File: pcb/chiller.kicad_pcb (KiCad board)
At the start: 2 copper layers, 62.2 x 55.1 mm, 45 parts, among them J1 CONN_01X03, J10 CONN_01X03, J11 CONN_01X02, J12 CONN_01X02, J2 CONN_01X03, J3 CONN_01X03, J4 CONN_01X02, J5 CONN_01X02, J6 CONN_01X02, J7 CONN_01X02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

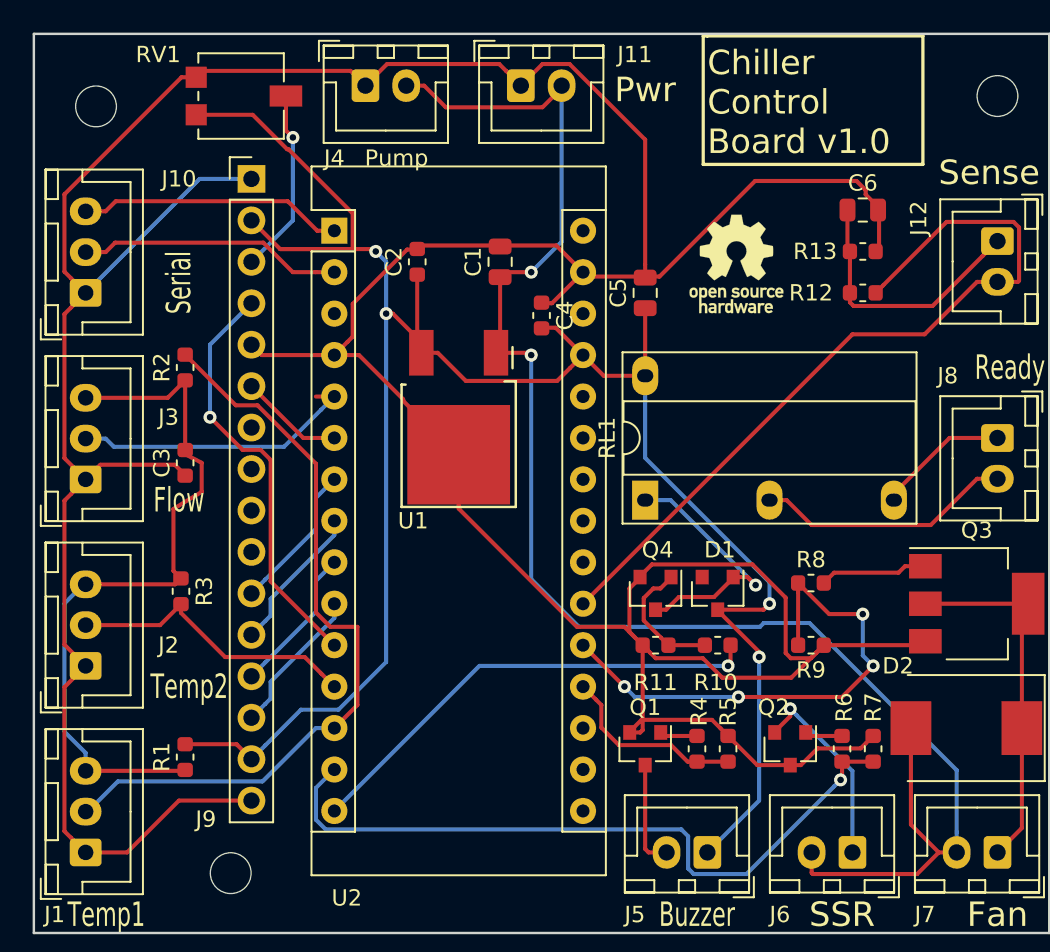
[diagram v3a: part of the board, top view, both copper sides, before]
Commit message: Fix errors: - Relay wrong footprint - Q2 switched D and G
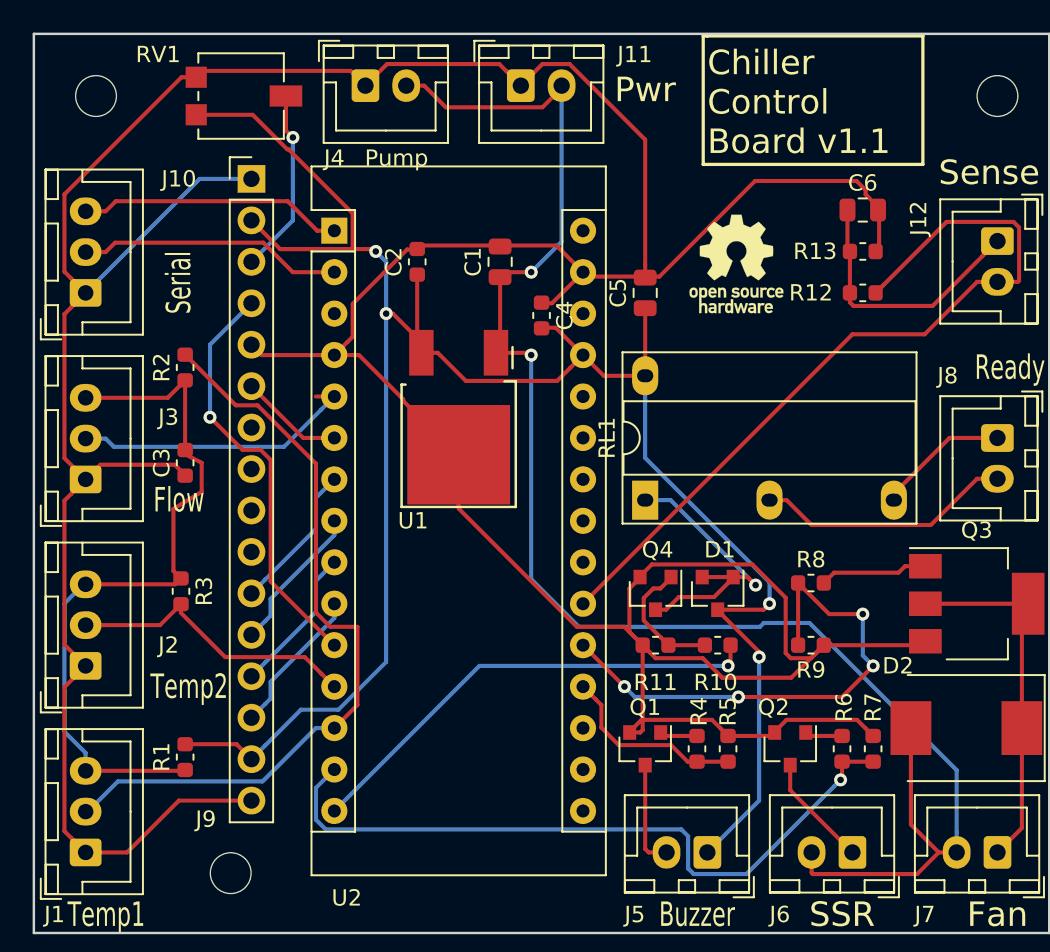
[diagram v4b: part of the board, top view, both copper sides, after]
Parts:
- moved REF** 0.64 mm to (183.5, 52.7)
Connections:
- D1 pad 2: (no net) -> Net-(D1-Pad1)
- Q2 pad 2: Net-(J6-Pad1) -> GND
- Q2 pad 3: GND -> Net-(J6-Pad1)
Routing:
- net Net-(J6-Pad1): track 12.2 -> 6.93 mm, vias 1 -> 0
- net Net-(D1-Pad1): track 16.1 -> 18.0 mm
- net GND: track 270.3 -> 269.7 mm
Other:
- rule pad_to_mask_clearance: 0.2 -> -0.2
- board text added: "Chiller Control Board v1.1"
- board text removed: "Chiller Control Board v1.0"
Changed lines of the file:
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@@
-(kicad_pcb (version 20171130) (host pcbnew 5.0.0-fee4fd1~66~ubuntu16.04.1)
+(kicad_pcb (version 20171130) (host pcbnew 5.0.2-bee76a0~70~ubuntu18.04.1)
   (general
     (thickness 1.6)
     (drawings 22)
-    (tracks 392)
+    (tracks 388)
     (zones 0)
     (modules 45)
@@
   (page A4)
   (layers
-    (0 F.Cu signal hide)
+    (0 F.Cu signal)
     (31 B.Cu signal)
     (32 B.Adhes user)
@@
     (pad_size 1.524 1.524)
     (pad_drill 0.762)
-    (pad_to_mask_clearance 0.2)
+    (pad_to_mask_clearance -0.2)
+    (solder_mask_min_width 0.25)
     (aux_axis_origin 0 0)
     (visible_elements FFFFFF7F)
     (pcbplotparams
-      (layerselection 0x010fc_ffffffff)
+      (layerselection 0x00008_7ffffffe)
       (usegerberextensions false)
       (usegerberattributes false)
@@
       (padsonsilk false)
       (subtractmaskfromsilk false)
-      (outputformat 1)
+      (outputformat 5)
       (mirror false)
       (drillshape 0)
@@
     (pad 3 smd rect (at 1 0 270) (size 0.9 0.8) (layers F.Cu F.Paste F.Mask)
       (net 3 +5V))
-    (pad 2 smd rect (at -1 0.95 270) (size 0.9 0.8) (layers F.Cu F.Paste F.Mask))
+    (pad 2 smd rect (at -1 0.95 270) (size 0.9 0.8) (layers F.Cu F.Paste F.Mask)
+      (net 24 "Net-(D1-Pad1)"))
     (pad 1 smd rect (at -1 -0.95 270) (size 0.9 0.8) (layers F.Cu F.Paste F.Mask)
       (net 24 "Net-(D1-Pad1)"))
@@
       (net 29 "Net-(Q2-Pad1)"))
     (pad 2 smd rect (at -1 0.95 270) (size 0.9 0.8) (layers F.Cu F.Paste F.Mask)
+      (net 1 GND))
+    (pad 3 smd rect (at 1 0 270) (size 0.9 0.8) (layers F.Cu F.Paste F.Mask)
       (net 26 "Net-(J6-Pad1)"))
-    (pad 3 smd rect (at 1 0 270) (size 0.9 0.8) (layers F.Cu F.Paste F.Mask)
-      (net 1 GND))
     (model ${KISYS3DMOD}/Package_TO_SOT_SMD.3dshapes/SOT-23.wrl
       (at (xyz 0 0 0))
@@
   )
   (module MountingHole:MountingHole_2.5mm (layer F.Cu)
-    (at 183.515 53.34)
+    (at 183.515 52.705)
     (descr "Mounting Hole 2.5mm, no annular")
     (tags "mounting hole 2.5mm no annular")
@@
   (gr_line (start 234.188 49.022) (end 234.188 56.896) (layer F.SilkS) (width 0.2))
   (gr_line (start 220.98 49.022) (end 234.188 49.022) (layer F.SilkS) (width 0.2))
-  (gr_text "Chiller\nControl\nBoard v1.0" (at 220.98 53.086) (layer F.SilkS)
+  (gr_text "Chiller\nControl\nBoard v1.1" (at 220.98 53.086) (layer F.SilkS)
     (effects (font (size 1.5 1.5) (thickness 0.3)) (justify left))
   )
@@
   (segment (start 216.22 91.66) (end 216.945001 90.934999) (width 0.25) (layer F.Cu) (net 1))
   (segment (start 216.22 91.71) (end 216.22 91.66) (width 0.25) (layer F.Cu) (net 1))
-  (segment (start 224.0375 93.71) (end 226.06 93.71) (width 0.25) (layer F.Cu) (net 1))
-  (segment (start 222.25 91.9225) (end 224.0375 93.71) (width 0.25) (layer F.Cu) (net 1))
-  (segment (start 230.678388 92.384112) (end 231.14 91.9225) (width 0.25) (layer F.Cu) (net 1))
-  (segment (start 230.37749 92.68501) (end 230.678388 92.384112) (width 0.25) (layer F.Cu) (net 1))
-  (segment (start 227.73499 92.68501) (end 230.37749 92.68501) (width 0.25) (layer F.Cu) (net 1))
-  (segment (start 226.71 93.71) (end 227.73499 92.68501) (width 0.25) (layer F.Cu) (net 1))
-  (segment (start 226.06 93.71) (end 226.71 93.71) (width 0.25) (layer F.Cu) (net 1))
   (segment (start 216.555888 85.898388) (end 217.0175 86.36) (width 0.25) (layer F.Cu) (net 1))
   (segment (start 212.984999 85.234999) (end 215.892499 85.234999) (width 0.25) (layer F.Cu) (net 1))
@@
   (segment (start 230.679999 58.739999) (end 230.679999 58.467999) (width 0.25) (layer F.Cu) (net 1))
   (segment (start 231.505 59.565) (end 230.679999 58.739999) (width 0.25) (layer F.Cu) (net 1))
+  (segment (start 222.25 91.9225) (end 224.8975 91.9225) (width 0.25) (layer F.Cu) (net 1) (status C00000))
+  (segment (start 224.8975 91.9225) (end 225.11 91.71) (width 0.25) (layer F.Cu) (net 1) (status C00000))
+  (segment (start 230.152499 90.934999) (end 230.678388 91.460888) (width 0.25) (layer F.Cu) (net 1))
+  (segment (start 230.678388 91.460888) (end 231.14 91.9225) (width 0.25) (layer F.Cu) (net 1))
+  (segment (start 225.835001 90.934999) (end 230.152499 90.934999) (width 0.25) (layer F.Cu) (net 1))
+  (segment (start 225.11 91.66) (end 225.835001 90.934999) (width 0.25) (layer F.Cu) (net 1))
+  (segment (start 225.11 91.71) (end 225.11 91.66) (width 0.25) (layer F.Cu) (net 1))
   (segment (start 208.28 68.186) (end 208.026 68.44) (width 0.25) (layer F.Cu) (net 2))
   (segment (start 208.28 63.865) (end 208.28 68.186) (width 0.25) (layer F.Cu) (net 2))
@@
   (segment (start 218.729682 77.47) (end 223.537337 82.277655) (width 0.25) (layer B.Cu) (net 24))
   (segment (start 223.444682 82.185) (end 223.537337 82.277655) (width 0.25) (layer F.Cu) (net 24))
+  (segment (start 220.665 82.185) (end 222.565 82.185) (width 0.25) (layer F.Cu) (net 24))
   (segment (start 217.38 99.06) (end 218.48 99.06) (width 0.25) (layer F.Cu) (net 25))
   (segment (start 217.17 98.85) (end 217.38 99.06) (width 0.25) (layer F.Cu) (net 25))
   (segment (start 217.17 93.71) (end 217.17 98.85) (width 0.25) (layer F.Cu) (net 25))
-  (via (at 226.06 90.26001) (size 0.8) (drill 0.4) (layers F.Cu B.Cu) (net 26))
-  (segment (start 226.459999 90.660009) (end 226.06 90.26001) (width 0.25) (layer B.Cu) (net 26))
-  (segment (start 225.11 91.66) (end 226.06 90.71) (width 0.25) (layer F.Cu) (net 26))
-  (segment (start 226.06 90.71) (end 226.06 90.26001) (width 0.25) (layer F.Cu) (net 26))
-  (segment (start 229.87 99.06) (end 229.87 94.07001) (width 0.25) (layer B.Cu) (net 26))
-  (segment (start 225.11 91.71) (end 225.11 91.66) (width 0.25) (layer F.Cu) (net 26))
-  (segment (start 229.87 94.07001) (end 226.459999 90.660009) (width 0.25) (layer B.Cu) (net 26))
+  (segment (start 226.06 95.25) (end 229.87 99.06) (width 0.25) (layer F.Cu) (net 26))
+  (segment (start 226.06 93.71) (end 226.06 95.25) (width 0.25) (layer F.Cu) (net 26))
   (segment (start 195.155 54.82) (end 195.58 55.245) (width 0.25) (layer F.Cu) (net 27))
   (via (at 195.58 55.245) (size 0.8) (drill 0.4) (layers F.Cu B.Cu) (net 27))

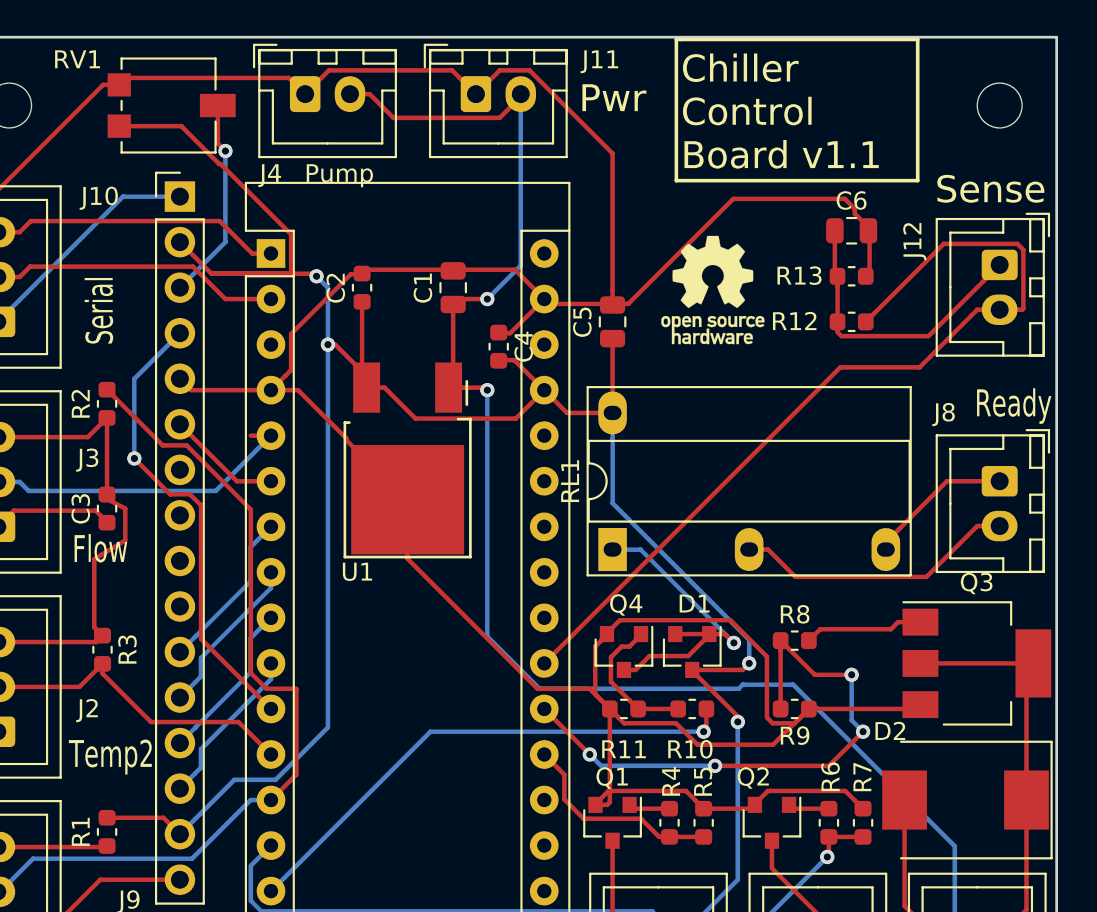
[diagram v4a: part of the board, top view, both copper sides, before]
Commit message: Update potentiometer and relay footprints.
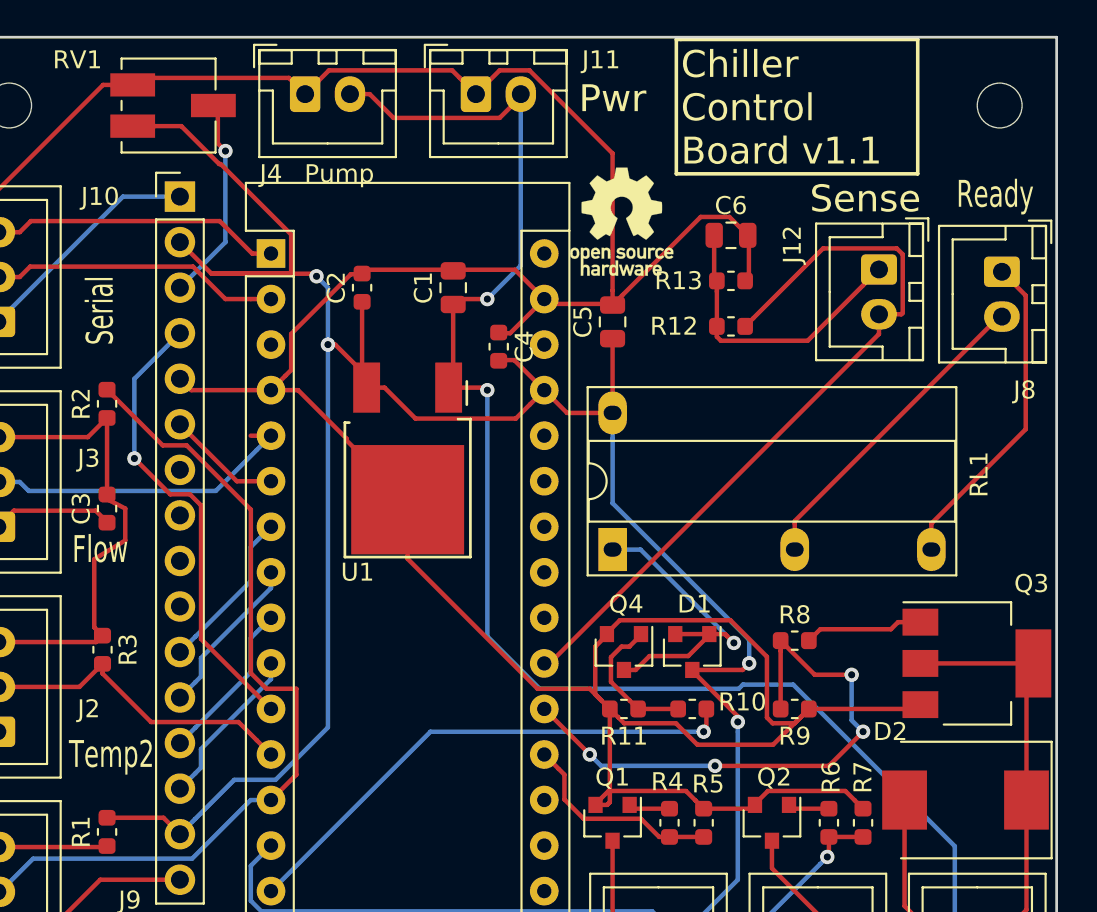
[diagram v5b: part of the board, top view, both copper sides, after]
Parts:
- moved J8 11.7 mm to (238.9, 62.0)
- moved C6 6.74 mm to (223.8, 59.9)
- moved J12 6.74 mm to (232.0, 61.8)
- moved R12 6.74 mm to (223.8, 65.0)
- moved R13 6.74 mm to (223.8, 62.5)
- moved REF** 6.35 mm to (217.7, 59.2)
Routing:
- net Net-(J8-Pad1): track 8.16 -> 18.2 mm
- net GND: track 269.7 -> 262.1 mm
- net A2: track 48.9 -> 42.7 mm
- net Net-(J8-Pad2): track 15.8 -> 17.9 mm

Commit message: Update to KiCad 5 format.
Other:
- net class Default removed
